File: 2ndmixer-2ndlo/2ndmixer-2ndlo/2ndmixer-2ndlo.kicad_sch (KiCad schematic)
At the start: 58 parts, among them J201 Coax Solder Point, J202 Conn_01x02, J203 Coax Solder Point, Q201 2N5179, Q202 2N5179, T201 Bifilar_Transformer, U201 MAV-11BSM+, U202 TUF-1H+, Y201 100MHz

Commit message: 2ndmixer-2ndlo bom and corrections
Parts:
- removed U201: MAV-11BSM+, 2ndmixer-2ndlo:MAV-11BSM&plus_, symbol 2022-08-04_19-42-18:MAV-11BSM+
- added U201: MAV-11, 2ndmixer-2ndlo:MAV-11BSM&plus_, symbol 2ndmixer-2ndlo:MAV-11
- C201, C203: value 470u -> 470p
- C204, C205: value 33 -> 33p
- C206: value 10u-50u -> 12p-60p
- C207: value 15 -> 15p
- C208: value 82 -> 82p
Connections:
- net GND: now also U201.2 (GND), U201.3 (RF_Out), U201.4 (GND)
- net at C209.2, TP206.1: now also U201.1 (RF_In)

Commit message: minor fix to 2ndmixer-2ndlo
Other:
- note removed: "Notes: -Digikey does not have 82u caps -Seems like 100Mhz 5th overtone xtal is special order -MAV-11 is available but not on Digi-Key and as a surface mount -TUF-1H+ not on Digi-Key but avaialble from MiniCircuits"
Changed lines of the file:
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@@
     (stroke (width 0) (type default) (color 0 0 0 0))
-  )
-  (text "Notes:\n-Digikey does not have 82u caps\n-Seems like 100Mhz 5th overtone xtal is special order\n-MAV-11 is available but not on Digi-Key and as a surface mount\n-TUF-1H+ not on Digi-Key but avaialble from MiniCircuits\n"
-    (at 16.51 196.85 0)
-    (effects (font (size 1.27 1.27)) (justify left bottom))
   )
   (text "6db Pad" (at 132.08 133.985 0)

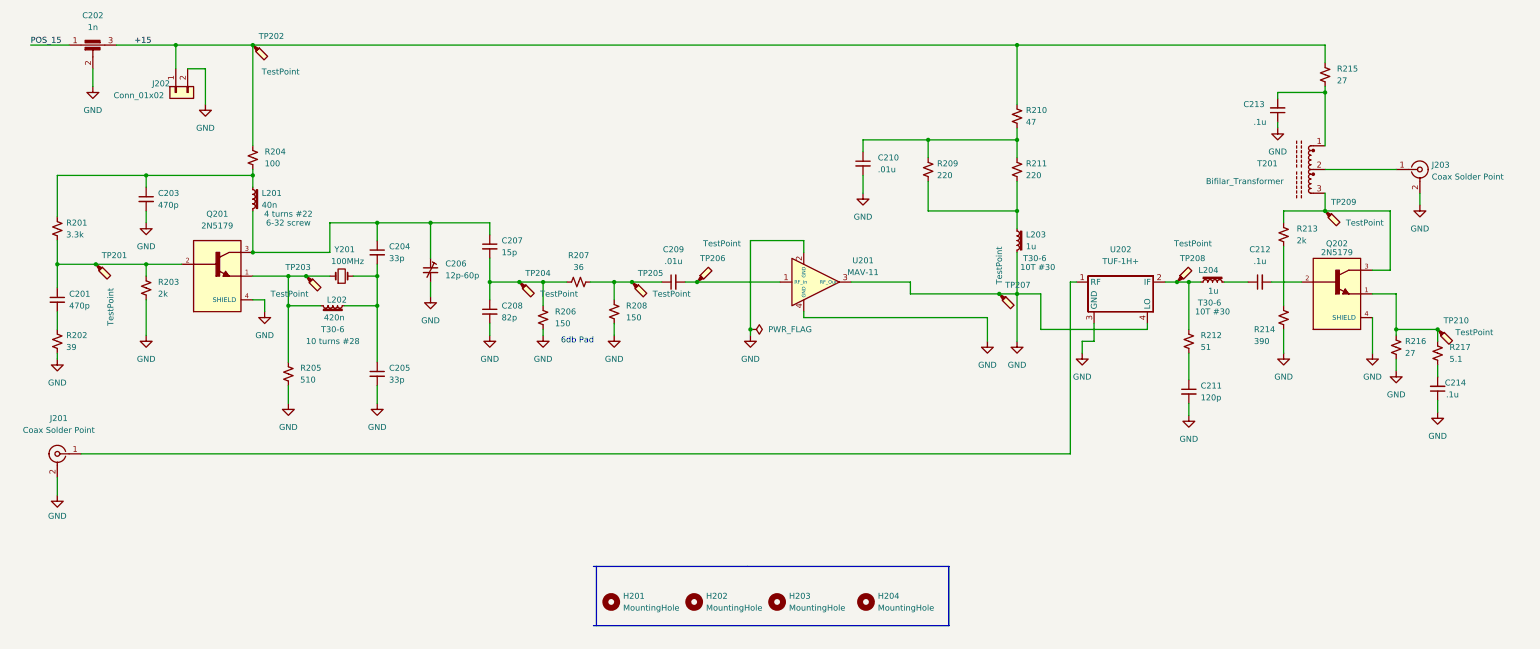
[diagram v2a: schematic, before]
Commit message: Hierarchical schematic updates
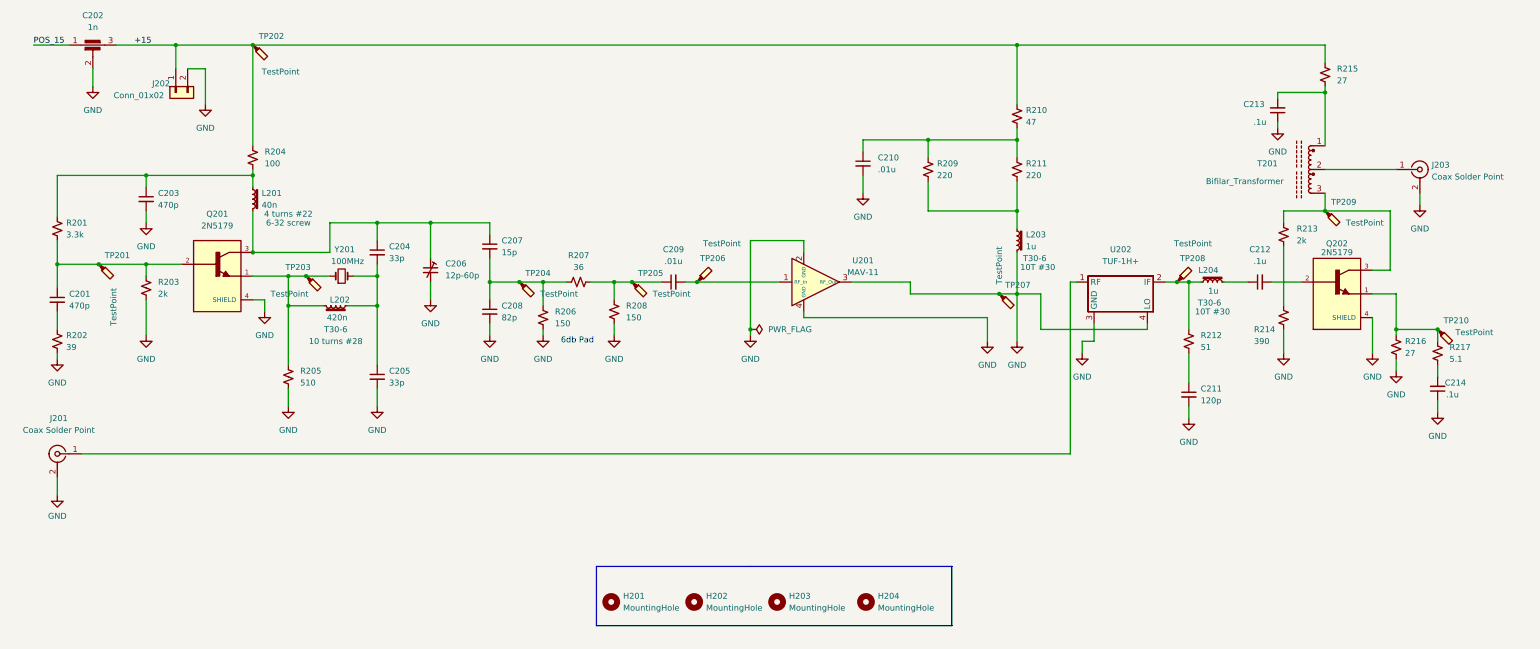
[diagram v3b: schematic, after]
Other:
- moved on the sheet: C205, C211, L202, R205, TP201

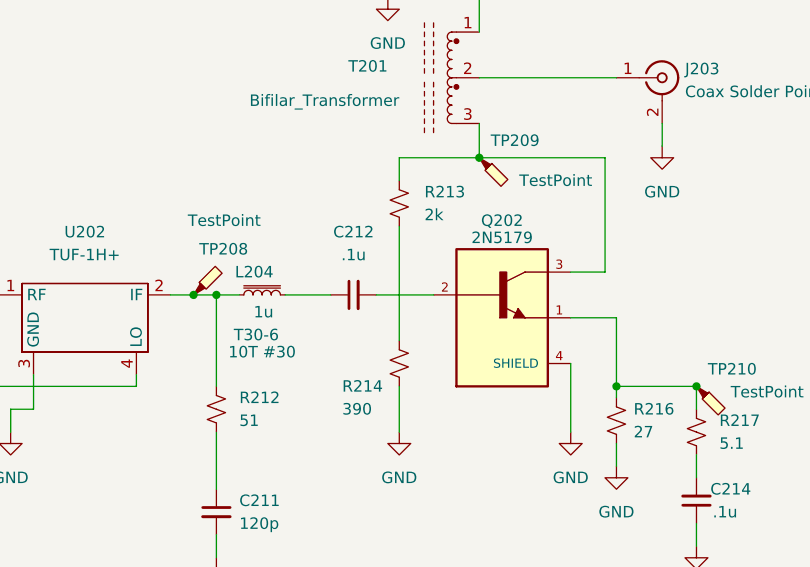
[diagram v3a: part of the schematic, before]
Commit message: added junction at base of 2N5179
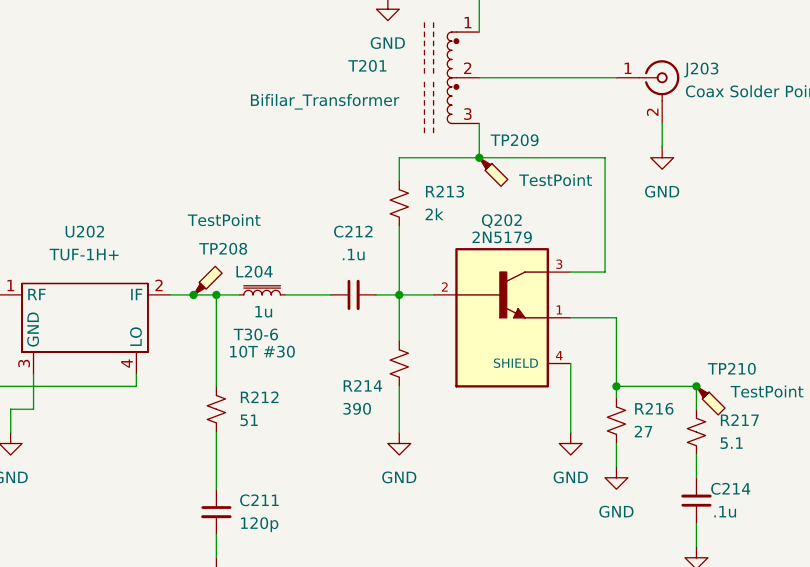
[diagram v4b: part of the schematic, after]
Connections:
- net at C212.2, Q202.2: now also R213.2, R214.1
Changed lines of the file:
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@@
   (junction (at 295.91 105.41) (diameter 0) (color 0 0 0 0)
   )
+  (junction (at 287.02 120.65) (diameter 0) (color 0 0 0 0)
+  )
   (junction (at 66.04 114.3) (diameter 0) (color 0 0 0 0)
   )
@@
     (stroke (width 0) (type default) (color 0 0 0 0))
   )
+  (wire (pts (xy 287.02 120.65) (xy 290.83 120.65))
+    (stroke (width 0) (type default) (color 0 0 0 0))
+  )
   (wire (pts (xy 229.87 114.3) (xy 229.87 123.19))
     (stroke (width 0) (type default) (color 0 0 0 0))
@@
     (stroke (width 0) (type default) (color 0 0 0 0))
   )
-  (wire (pts (xy 287.02 113.03) (xy 287.02 125.73))
+  (wire (pts (xy 287.02 113.03) (xy 287.02 120.65))
     (stroke (width 0) (type default) (color 0 0 0 0))
   )
@@
     (stroke (width 0) (type default) (color 0 0 0 0))
   )
+  (wire (pts (xy 287.02 120.65) (xy 287.02 125.73))
+    (stroke (width 0) (type default) (color 0 0 0 0))
+  )
   (wire (pts (xy 158.75 120.65) (xy 161.29 120.65))
     (stroke (width 0) (type default) (color 0 0 0 0))
@@
     (stroke (width 0) (type default) (color 0 0 0 0))
   )
-  (wire (pts (xy 284.48 120.65) (xy 290.83 120.65))
-    (stroke (width 0) (type default) (color 0 0 0 0))
-  )
+  (wire (pts (xy 284.48 120.65) (xy 287.02 120.65))
+    (stroke (width 0) (type default) (color 0 0 0 0))
+  )

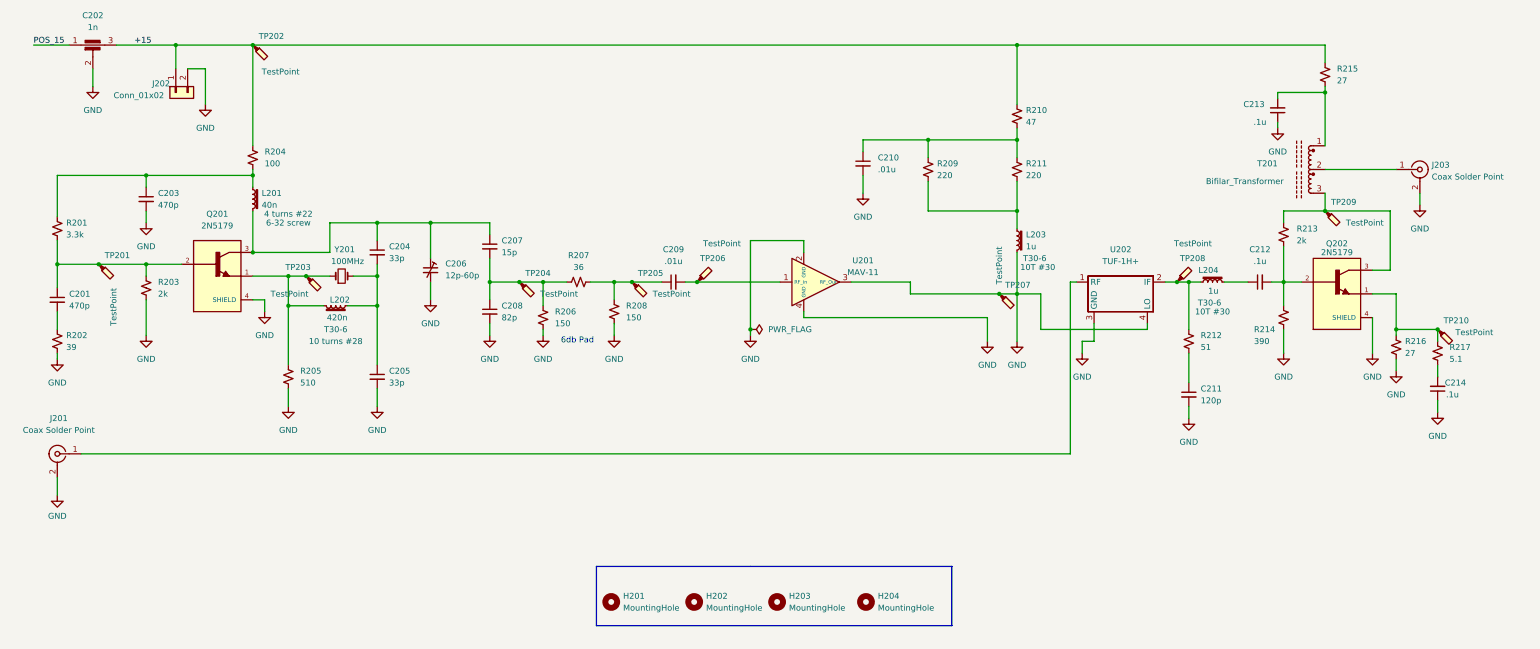
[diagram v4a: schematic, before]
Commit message: minor changes to 5 boards
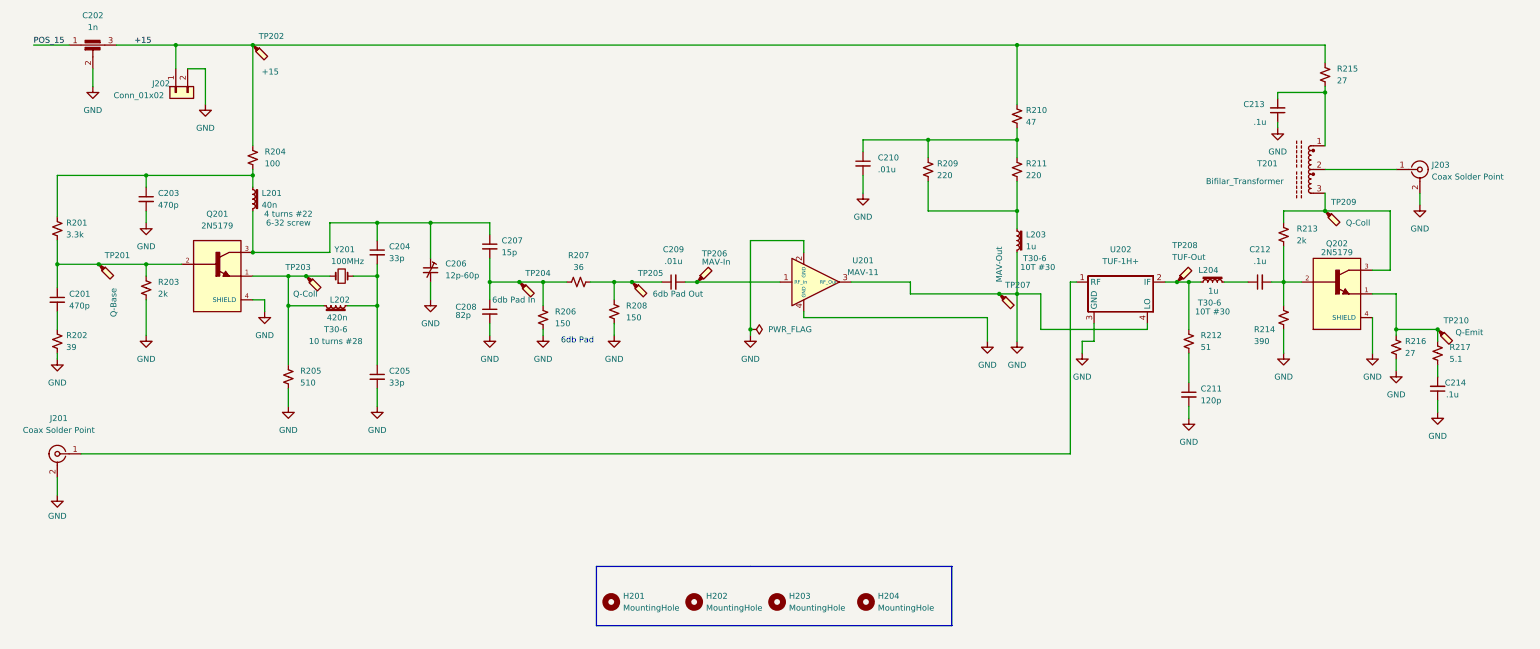
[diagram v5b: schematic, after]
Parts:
- TP201: value TestPoint -> Q-Base
- TP202: value TestPoint -> +15
- TP203, TP209: value TestPoint -> Q-Coll
- TP204: value TestPoint -> 6db Pad In
- TP205: value TestPoint -> 6db Pad Out
- TP206: value TestPoint -> MAV-In
- TP207: value TestPoint -> MAV-Out
- TP208: value TestPoint -> TUF-Out
- TP210: value TestPoint -> Q-Emit
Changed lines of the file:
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@@
   (symbol (lib_id "Connector:TestPoint_Probe") (at 161.29 120.65 270) (mirror x) (unit 1)
     (in_bom yes) (on_board yes)
-    (property "Reference" "TP206" (id 0) (at 161.925 115.57 90)
-      (effects (font (size 1.27 1.27)) (justify left))
-    )
-    (property "Value" "TestPoint" (id 1) (at 162.56 112.395 90)
+    (property "Reference" "TP206" (id 0) (at 162.306 114.554 90)
+      (effects (font (size 1.27 1.27)) (justify left))
+    )
+    (property "Value" "MAV-In" (id 1) (at 162.306 116.332 90)
       (effects (font (size 1.27 1.27)) (justify left))
     )
@@
   (symbol (lib_id "Connector:TestPoint_Probe") (at 264.16 120.65 270) (mirror x) (unit 1)
     (in_bom yes) (on_board yes)
-    (property "Reference" "TP208" (id 0) (at 264.795 115.57 90)
-      (effects (font (size 1.27 1.27)) (justify left))
-    )
-    (property "Value" "TestPoint" (id 1) (at 263.525 112.395 90)
+    (property "Reference" "TP208" (id 0) (at 263.144 112.776 90)
+      (effects (font (size 1.27 1.27)) (justify left))
+    )
+    (property "Value" "TUF-Out" (id 1) (at 263.144 115.316 90)
       (effects (font (size 1.27 1.27)) (justify left))
     )
@@
       (effects (font (size 1.27 1.27)) (justify left))
     )
-    (property "Value" "TestPoint" (id 1) (at 127.635 123.19 0)
+    (property "Value" "6db Pad In" (id 1) (at 117.348 124.46 0)
       (effects (font (size 1.27 1.27)) (justify left))
     )
@@
       (effects (font (size 1.27 1.27)) (justify left))
     )
-    (property "Value" "TestPoint" (id 1) (at 151.765 123.19 0)
+    (property "Value" "6db Pad Out" (id 1) (at 151.765 123.19 0)
       (effects (font (size 1.27 1.27)) (justify left))
     )
@@
   )
   (symbol (lib_id "Device:C_Small") (at 116.84 127 0) (unit 1)
-    (in_bom yes) (on_board yes) (fields_autoplaced)
-    (property "Reference" "C208" (id 0) (at 119.38 125.7362 0)
-      (effects (font (size 1.27 1.27)) (justify left))
-    )
-    (property "Value" "82p" (id 1) (at 119.38 128.2762 0)
+    (in_bom yes) (on_board yes)
+    (property "Reference" "C208" (id 0) (at 109.474 125.984 0)
+      (effects (font (size 1.27 1.27)) (justify left))
+    )
+    (property "Value" "82p" (id 1) (at 109.474 127.762 0)
       (effects (font (size 1.27 1.27)) (justify left))
     )
@@
       (effects (font (size 1.27 1.27)) (justify left))
     )
-    (property "Value" "TestPoint" (id 1) (at 300.355 107.95 0)
+    (property "Value" "Q-Coll" (id 1) (at 300.355 107.95 0)
       (effects (font (size 1.27 1.27)) (justify left))
     )
@@
       (effects (font (size 1.27 1.27)) (justify left))
     )
-    (property "Value" "TestPoint" (id 1) (at 36.195 121.92 90)
+    (property "Value" "Q-Base" (id 1) (at 36.195 121.92 90)
       (effects (font (size 1.27 1.27)) (justify left))
     )
@@
       (effects (font (size 1.27 1.27)) (justify left))
     )
-    (property "Value" "TestPoint" (id 1) (at 67.945 75.565 0)
+    (property "Value" "+15" (id 1) (at 67.945 75.565 0)
       (effects (font (size 1.27 1.27)) (justify left))
     )
@@
       (effects (font (size 1.27 1.27)) (justify left))
     )
-    (property "Value" "TestPoint" (id 1) (at 69.85 123.19 0)
+    (property "Value" "Q-Coll" (id 1) (at 74.676 123.19 0)
       (effects (font (size 1.27 1.27)) (justify left))
     )
@@
       (effects (font (size 1.27 1.27)) (justify left))
     )
-    (property "Value" "TestPoint" (id 1) (at 226.06 113.03 90)
+    (property "Value" "MAV-Out" (id 1) (at 226.06 113.03 90)
       (effects (font (size 1.27 1.27)) (justify left))
     )
@@
       (effects (font (size 1.27 1.27)) (justify left))
     )
-    (property "Value" "TestPoint" (id 1) (at 323.85 131.445 0)
+    (property "Value" "Q-Emit" (id 1) (at 323.85 131.445 0)
       (effects (font (size 1.27 1.27)) (justify left))
     )
@@
     )
     (path "/7b11a78d-717b-4bb1-ae80-7cd31e4ce39d"
-      (reference "TP201") (unit 1) (value "TestPoint") (footprint "TestPoint:TestPoint_Pad_1.0x1.0mm")
+      (reference "TP201") (unit 1) (value "Q-Base") (footprint "TestPoint:TestPoint_Pad_1.0x1.0mm")
     )
     (path "/80f6f8fc-2b77-4791-9114-f12245dbc81a"
-      (reference "TP202") (unit 1) (value "TestPoint") (footprint "TestPoint:TestPoint_Pad_1.0x1.0mm")
+      (reference "TP202") (unit 1) (value "+15") (footprint "TestPoint:TestPoint_Pad_1.0x1.0mm")
     )
     (path "/b3d99b90-a563-46c4-8df2-ec7449e34af7"
-      (reference "TP203") (unit 1) (value "TestPoint") (footprint "TestPoint:TestPoint_Pad_1.0x1.0mm")
+      (reference "TP203") (unit 1) (value "Q-Coll") (footprint "TestPoint:TestPoint_Pad_1.0x1.0mm")
     )
     (path "/3076ed7b-0b06-4ea4-ba72-ad5a1845b382"
-      (reference "TP204") (unit 1) (value "TestPoint") (footprint "TestPoint:TestPoint_Pad_1.0x1.0mm")
+      (reference "TP204") (unit 1) (value "6db Pad In") (footprint "TestPoint:TestPoint_Pad_1.0x1.0mm")
     )
     (path "/38003388-8080-4693-82ad-14b5f8202bb9"
-      (reference "TP205") (unit 1) (value "TestPoint") (footprint "TestPoint:TestPoint_Pad_1.0x1.0mm")
+      (reference "TP205") (unit 1) (value "6db Pad Out") (footprint "TestPoint:TestPoint_Pad_1.0x1.0mm")
     )
     (path "/1ba743c0-435c-46d5-a953-07f7d610e39d"
-      (reference "TP206") (unit 1) (value "TestPoint") (footprint "TestPoint:TestPoint_Pad_1.0x1.0mm")
+      (reference "TP206") (unit 1) (value "MAV-In") (footprint "TestPoint:TestPoint_Pad_1.0x1.0mm")
     )
     (path "/b7bb0979-8cc2-409c-89a9-b3f934688d3c"
-      (reference "TP207") (unit 1) (value "TestPoint") (footprint "TestPoint:TestPoint_Pad_1.0x1.0mm")
+      (reference "TP207") (unit 1) (value "MAV-Out") (footprint "TestPoint:TestPoint_Pad_1.0x1.0mm")
     )
     (path "/233649c1-f208-4454-b44c-33496ae14eec"
-      (reference "TP208") (unit 1) (value "TestPoint") (footprint "TestPoint:TestPoint_Pad_1.0x1.0mm")
+      (reference "TP208") (unit 1) (value "TUF-Out") (footprint "TestPoint:TestPoint_Pad_1.0x1.0mm")
     )
     (path "/62d3c5be-6f3b-4ad9-81f6-486116ec53b5"
-      (reference "TP209") (unit 1) (value "TestPoint") (footprint "TestPoint:TestPoint_Pad_1.0x1.0mm")
+      (reference "TP209") (unit 1) (value "Q-Coll") (footprint "TestPoint:TestPoint_Pad_1.0x1.0mm")
     )
     (path "/d3bb7f25-1006-43ac-a22f-03cbe6a0bb45"
-      (reference "TP210") (unit 1) (value "TestPoint") (footprint "TestPoint:TestPoint_Pad_1.0x1.0mm")
+      (reference "TP210") (unit 1) (value "Q-Emit") (footprint "TestPoint:TestPoint_Pad_1.0x1.0mm")
     )
     (path "/2b269c59-d9c7-4321-a64d-f838ca5a5591"

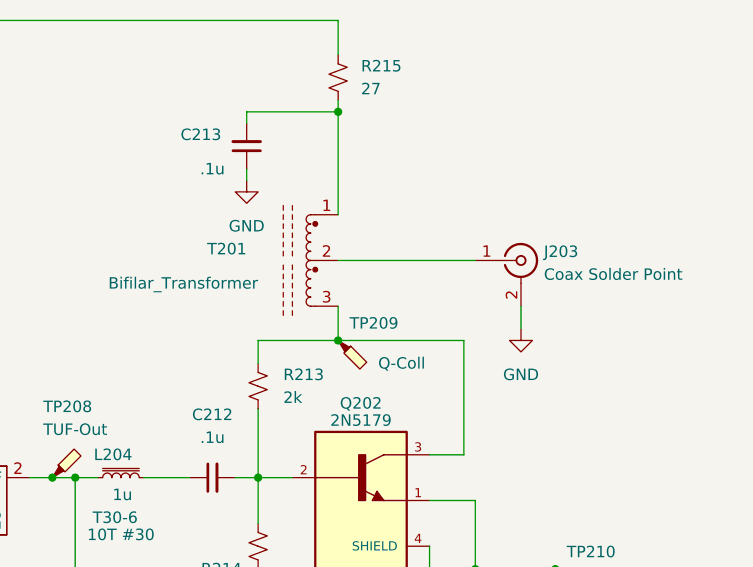
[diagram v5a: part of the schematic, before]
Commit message: Fix POS200 footprint and Terminal Block footprint of VCO 1st Mixer Board.  Rev 1.
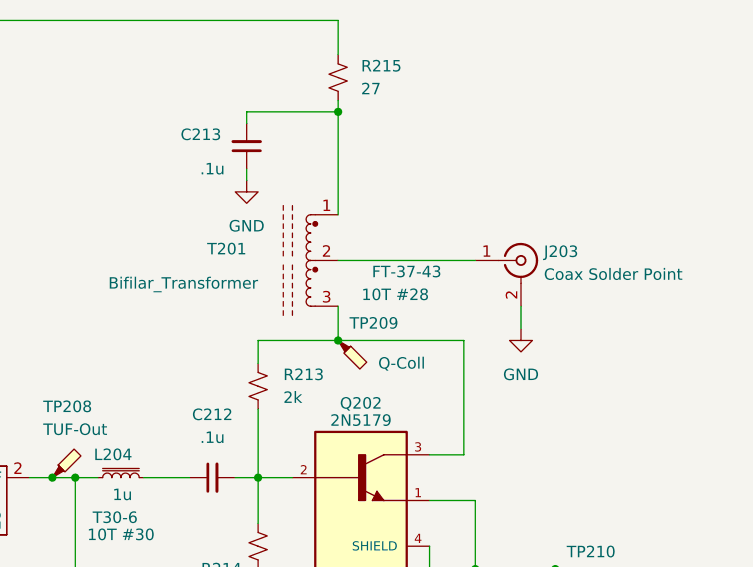
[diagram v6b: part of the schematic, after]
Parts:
- T201: Field4 (none) -> FT-37-43; Field5 (none) -> 10T #28
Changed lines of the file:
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@@
       (effects (font (size 1.27 1.27)) hide)
     )
+    (property "Field4" "FT-37-43 " (id 4) (at 303.53 97.79 90))
+    (property "Field5" "10T #28" (id 5) (at 302.26 100.33 90))
     (pin "1")
     (pin "2")
